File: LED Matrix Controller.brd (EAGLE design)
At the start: 76.2 x 50.8 mm, 8 parts, among them J1 5V PWR, J2 LED OUT, J3 AVR ISP, J4 SER DBG, U1 328P

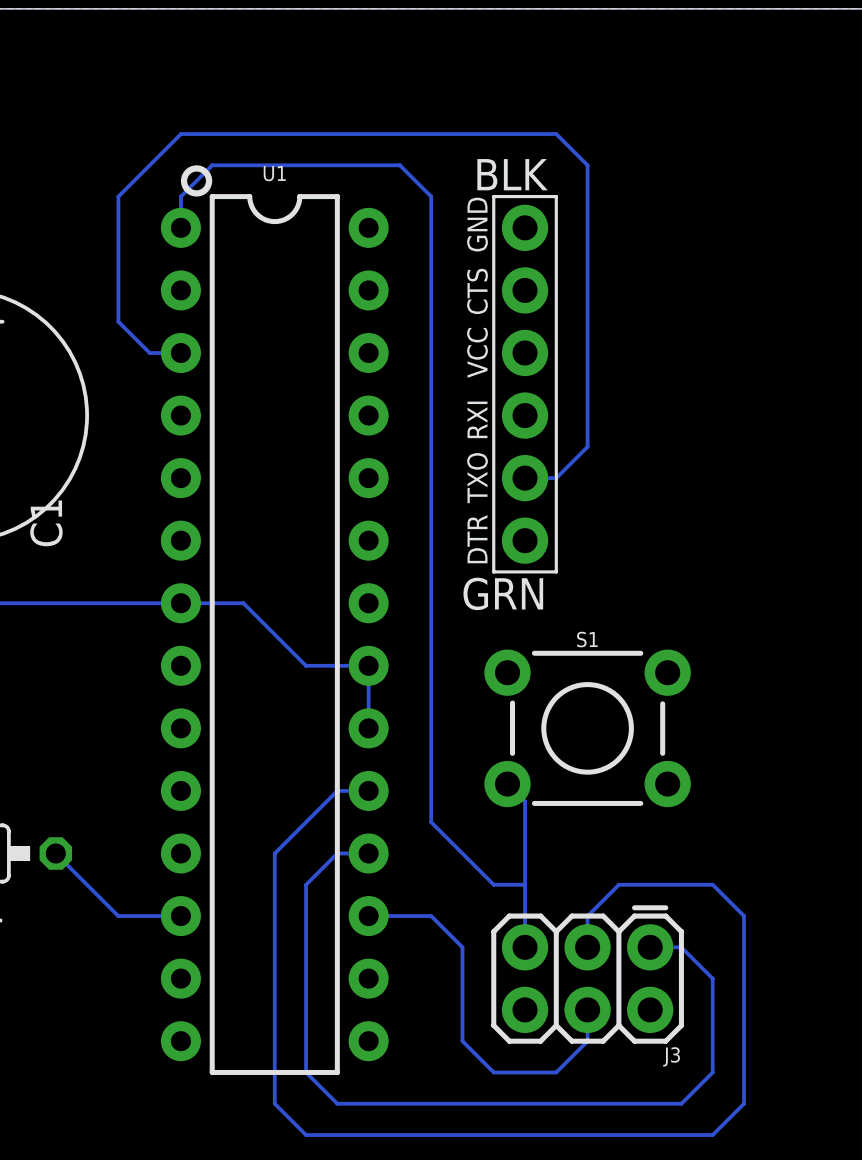
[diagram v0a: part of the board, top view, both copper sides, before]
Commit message: Create a two-layer version
A couple of small updates for manufacturing a 2 layer board.  Route
power to the ICSP header and the rest of the FTDI serial header
signals since it's easy now.
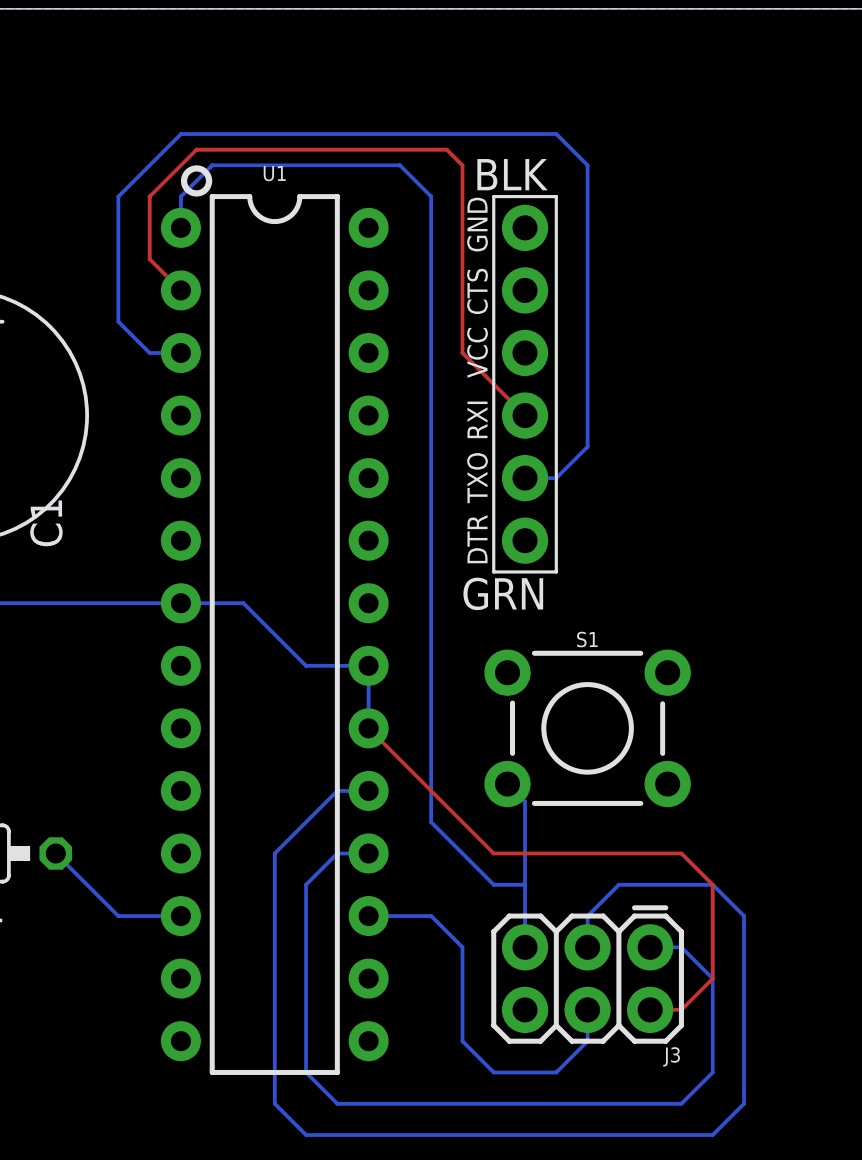
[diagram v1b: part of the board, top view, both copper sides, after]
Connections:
- new net N$3: J4.P$1
- new net N$5: J4.P$5
- new net RXD: J4.P$3, U1.2
- net +5V: now also J3.2
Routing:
- net RXD: track 0.00 -> 29.3 mm
- net +5V: track 62.3 -> 85.8 mm
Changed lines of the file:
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@@
 <wire x1="3.81" y1="34.29" x2="7.62" y2="36.83" width="0.1524" layer="16"/>
 <wire x1="7.62" y1="36.83" x2="16.51" y2="36.83" width="0.1524" layer="16"/>
+<contactref element="J3" pad="2"/>
+<wire x1="44.45" y1="10.16" x2="45.72" y2="10.16" width="0.1524" layer="1"/>
+<wire x1="45.72" y1="10.16" x2="46.99" y2="11.43" width="0.1524" layer="1"/>
+<wire x1="46.99" y1="11.43" x2="46.99" y2="15.24" width="0.1524" layer="1"/>
+<wire x1="46.99" y1="15.24" x2="45.72" y2="16.51" width="0.1524" layer="1"/>
+<wire x1="38.1" y1="16.51" x2="45.72" y2="16.51" width="0.1524" layer="1"/>
+<wire x1="33.02" y1="21.59" x2="38.1" y2="16.51" width="0.1524" layer="1"/>
 </signal>
 <signal name="GND">
@@
 <wire x1="40.64" y1="31.75" x2="39.37" y2="31.75" width="0.1524" layer="16"/>
 </signal>
+<signal name="N$3">
+<contactref element="J4" pad="P$1"/>
+</signal>
+<signal name="N$5">
+<contactref element="J4" pad="P$5"/>
+</signal>
+<signal name="RXD">
+<contactref element="U1" pad="2"/>
+<contactref element="J4" pad="P$3"/>
+<wire x1="39.37" y1="34.29" x2="36.83" y2="36.83" width="0.1524" layer="1"/>
+<wire x1="36.83" y1="36.83" x2="36.83" y2="44.45" width="0.1524" layer="1"/>
+<wire x1="36.83" y1="44.45" x2="36.195" y2="45.085" width="0.1524" layer="1"/>
+<wire x1="26.035" y1="45.085" x2="24.13" y2="43.18" width="0.1524" layer="1"/>
+<wire x1="24.13" y1="43.18" x2="24.13" y2="40.64" width="0.1524" layer="1"/>
+<wire x1="24.13" y1="40.64" x2="25.4" y2="39.37" width="0.1524" layer="1"/>
+<wire x1="36.195" y1="45.085" x2="26.035" y2="45.085" width="0.1524" layer="1"/>
+</signal>
 </signals>
